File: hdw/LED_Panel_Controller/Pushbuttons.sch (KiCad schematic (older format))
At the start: 10 parts

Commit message: lots of schematic progress
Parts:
- removed U?: 74LVC1G17, TO_SOT_Packages_SMD:SOT-353_SC-70-5, symbol Custom_Library:74LVC1G17_Power
- added R?: 10k, Resistors_SMD:R_0402, symbol Custom_Library:R_Custom
- added U?: 74LVC1G97, Package_TO_SOT_SMD:SOT-363_SC-70-6, symbol Custom_Library:74LVC1G97_Power_BUF
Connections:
- net labels added: Cap_Touch_Power
- wire segments 12 -> 15
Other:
- moved on the sheet: C?, R?, SW?, U?

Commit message: made a lot more schematic progress
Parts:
- removed R?: 499, Resistors_SMD:R_0402, symbol Custom_Library:R_Custom
- added C?: 10nF, Capacitors_SMD:C_0402, symbol Custom_Library:C_Custom
- added C? (x2): 0.1uF, Capacitors_SMD:C_0402, symbol Custom_Library:C_Custom
- added C?: 10uF, Capacitors_SMD:C_0402, symbol Custom_Library:C_Custom
- added R? (x4): 1k, Resistors_SMD:R_0402, symbol Custom_Library:R_Custom
- added R? (x3): 10k, Resistors_SMD:R_0402, symbol Custom_Library:R_Custom
- added SW?: Cap_Touch, Custom Footprints Library:Capacitive_Touch_Pad, symbol Custom_Library:Cap_Touch
- added U?: AT42QT1010-TSHR, TO_SOT_Packages_SMD:SOT-23-6, symbol Sensor_Touch:AT42QT1010-TSHR
- added U?: 74LVC1G97, Package_TO_SOT_SMD:SOT-363_SC-70-6, symbol Custom_Library:74LVC1G97_Power_BUF
- C? (x4), R? (x2), U? (x2): Configuration (none) -> PUSH
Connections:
- net +3V3: now also C?.1, C?.1, U?.5 (VCC), U?.5 (VDD), U?.6 (SYNC)
- net GND: now also C?.2, C?.2, C?.2, R?.2, R?.2, U?.2 (GND), U?.2 (VSS), U?.3 (GND), U?.6 (GND)
- net at C?.2, U?.3 (SNSK): now also R?.1, R?.1
- net at SW?.1 (TP): now also R?.2, R?.2
- new net: R?.1, R?.2, U?.1 (OUT)
- new net: C?.2, R?.1, R?.1, U?.3 (SNSK)
- new net: C?.1, U?.4 (SNS)
- new net: R?.2, R?.2, SW?.1 (TP)
- new net: C?.1, R?.1, U?.1
- new net Cap_Touch_Mode: R?.1, U?.4

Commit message: added digikey pns, footprints, bom scrubbed
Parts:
- C? (x2): Digi-Key PN 490-13295-1-ND -> 399-3066-1-ND
- C? (x4): Digi-Key PN (none) -> 490-10701-1-ND
- C? (x2): Digi-Key PN 490-13211-1-ND -> 1276-1451-1-ND
- R? (x4): Digi-Key PN (none) -> RMCF0402FT1K00CT-ND
- U? (x2): Digi-Key PN (none) -> 1727-1772-1-ND
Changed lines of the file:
@@
 F 2 "Capacitors_SMD:C_0402" H 4038 1660 50  0001 C CNN
 F 3 "" H 4025 1910 50  0001 C CNN
-F 4 "490-13295-1-ND" H -790 -410 50  0001 C CNN "Digi-Key PN"
+F 4 "399-3066-1-ND" H -790 -410 50  0001 C CNN "Digi-Key PN"
 F 5 "0402" V 3610 1810 50  0000 C CNN "display_footprint"
 F 6 "50V" V 3510 1810 50  0000 C CNN "Voltage"
@@
 F 6 "X7R" H 7070 2170 50  0000 R CNN "Dielectric"
 F 7 "PUSH" H 7070 2090 50  0000 R CNN "Configuration"
+F 8 "490-10701-1-ND" H 7220 2270 50  0001 C CNN "Digi-Key PN"
 	1    7220 2270
 	1    0    0    -1
@@
 F 5 "6.3V" H 6300 2100 50  0000 R CNN "Voltage"
 F 6 "X5R" H 6300 2000 50  0000 R CNN "Dielectric"
-F 7 "490-13211-1-ND" H 6450 2100 50  0001 C CNN "Digi-Key PN"
+F 7 "1276-1451-1-ND" H 6450 2100 50  0001 C CNN "Digi-Key PN"
 F 8 "PUSH" H 6300 1920 50  0000 R CNN "Configuration"
 	1    6450 2100
@@
 F 3 "http://www.ti.com/lit/ds/symlink/sn74lvc1g97.pdf" H 7040 1810 50  0001 C CNN
 F 4 "PUSH" H 7150 1730 50  0000 C CNN "Configuration"
+F 5 "1727-1772-1-ND" H 6990 1810 50  0001 C CNN "Digi-Key PN"
 	1    6990 1810
 	1    0    0    -1
@@
 F 6 "X7R" H 4780 2440 50  0000 R CNN "Dielectric"
 F 7 "PUSH" H 4790 2720 50  0000 R CNN "Configuration"
+F 8 "490-10701-1-ND" H 4930 2540 50  0001 C CNN "Digi-Key PN"
 	1    4930 2540
 	1    0    0    -1
@@
 F 6 "1/16W" V 3500 1890 50  0000 C CNN "Wattage"
 F 7 "PUSH" V 3590 1890 50  0000 C CNN "Configuration"
+F 8 "RMCF0402FT1K00CT-ND" H 3200 1890 50  0001 C CNN "Digi-Key PN"
 	1    3200 1890
 	0    1    1    0
@@
 F 6 "1/16W" V 3500 1610 50  0000 C CNN "Wattage"
 F 7 "PUSH" V 3590 1610 50  0000 C CNN "Configuration"
+F 8 "RMCF0402FT1K00CT-ND" H 3200 1610 50  0001 C CNN "Digi-Key PN"
 	1    3200 1610
 	0    1    -1   0
@@
 F 2 "Capacitors_SMD:C_0402" H 4038 3660 50  0001 C CNN
 F 3 "" H 4025 3910 50  0001 C CNN
-F 4 "490-13295-1-ND" H -790 1590 50  0001 C CNN "Digi-Key PN"
+F 4 "399-3066-1-ND" H -790 1590 50  0001 C CNN "Digi-Key PN"
 F 5 "0402" V 3610 3810 50  0000 C CNN "display_footprint"
 F 6 "50V" V 3510 3810 50  0000 C CNN "Voltage"
@@
 F 6 "X7R" H 7070 4170 50  0000 R CNN "Dielectric"
 F 7 "PUSH" H 7070 4090 50  0000 R CNN "Configuration"
+F 8 "490-10701-1-ND" H 7220 4270 50  0001 C CNN "Digi-Key PN"
 	1    7220 4270
 	1    0    0    -1
@@
 F 5 "6.3V" H 6300 4100 50  0000 R CNN "Voltage"
 F 6 "X5R" H 6300 4000 50  0000 R CNN "Dielectric"
-F 7 "490-13211-1-ND" H 6450 4100 50  0001 C CNN "Digi-Key PN"
+F 7 "1276-1451-1-ND" H 6450 4100 50  0001 C CNN "Digi-Key PN"
 F 8 "PUSH" H 6300 3920 50  0000 R CNN "Configuration"
 	1    6450 4100
@@
 F 3 "http://www.ti.com/lit/ds/symlink/sn74lvc1g97.pdf" H 7040 3810 50  0001 C CNN
 F 4 "PUSH" H 7150 3730 50  0000 C CNN "Configuration"
+F 5 "1727-1772-1-ND" H 6990 3810 50  0001 C CNN "Digi-Key PN"
 	1    6990 3810
 	1    0    0    -1
@@
 F 6 "X7R" H 4780 4440 50  0000 R CNN "Dielectric"
 F 7 "PUSH" H 4790 4720 50  0000 R CNN "Configuration"
+F 8 "490-10701-1-ND" H 4930 4540 50  0001 C CNN "Digi-Key PN"
 	1    4930 4540
 	1    0    0    -1
@@
 F 6 "1/16W" V 3500 3890 50  0000 C CNN "Wattage"
 F 7 "PUSH" V 3590 3890 50  0000 C CNN "Configuration"
+F 8 "RMCF0402FT1K00CT-ND" H 3200 3890 50  0001 C CNN "Digi-Key PN"
 	1    3200 3890
 	0    1    1    0
@@
 F 6 "1/16W" V 3500 3610 50  0000 C CNN "Wattage"
 F 7 "PUSH" V 3590 3610 50  0000 C CNN "Configuration"
+F 8 "RMCF0402FT1K00CT-ND" H 3200 3610 50  0001 C CNN "Digi-Key PN"
 	1    3200 3610
 	0    1    -1   0

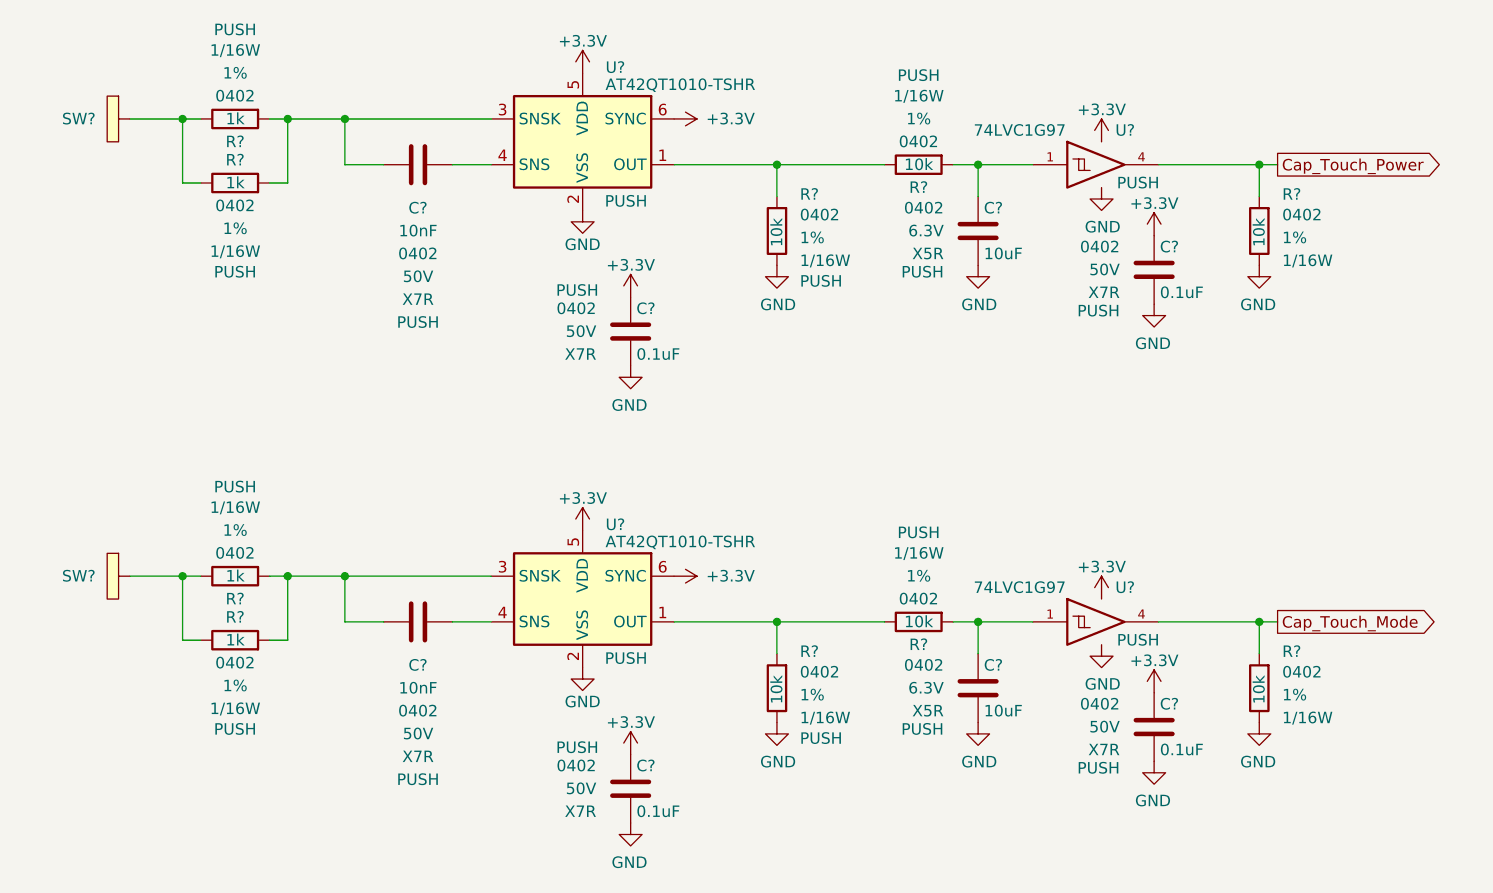
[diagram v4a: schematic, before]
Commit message: assigned I2C addresses
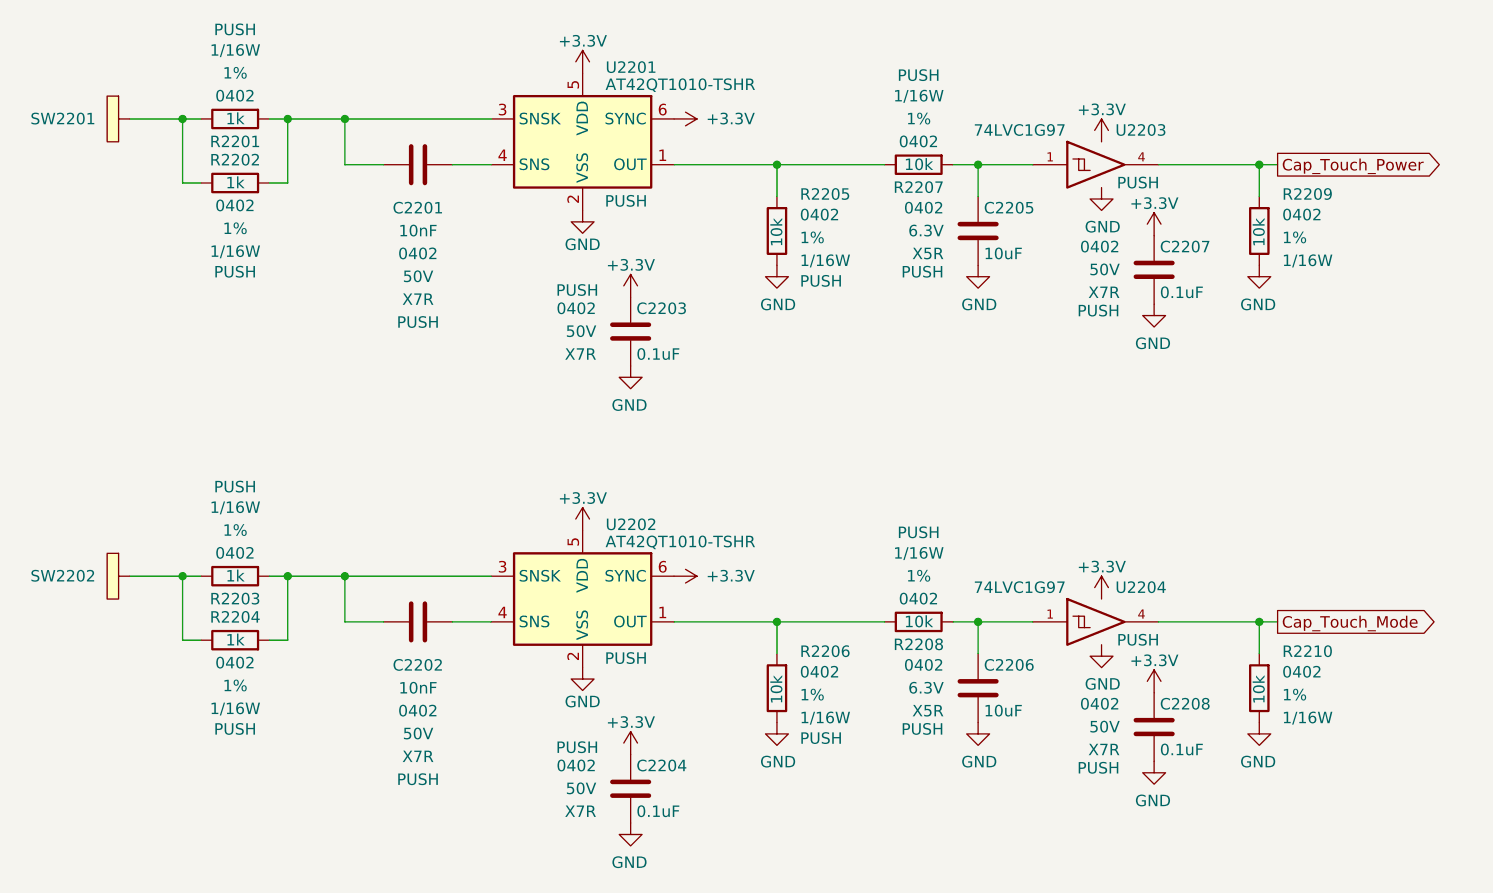
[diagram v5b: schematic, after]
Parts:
- gave numbers to parts that had none: 24

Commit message: added BOMs, some consolidation
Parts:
- C2203, C2204, C2207, C2208: Digi-Key PN 490-10701-1-ND -> 490-10698-1-ND
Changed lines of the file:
@@
 F 6 "X7R" H 7070 2170 50  0000 R CNN "Dielectric"
 F 7 "PUSH" H 7070 2090 50  0000 R CNN "Configuration"
-F 8 "490-10701-1-ND" H 7220 2270 50  0001 C CNN "Digi-Key PN"
+F 8 "490-10698-1-ND" H 7220 2270 50  0001 C CNN "Digi-Key PN"
 	1    7220 2270
 	1    0    0    -1
@@
 F 6 "X7R" H 4780 2440 50  0000 R CNN "Dielectric"
 F 7 "PUSH" H 4790 2720 50  0000 R CNN "Configuration"
-F 8 "490-10701-1-ND" H 4930 2540 50  0001 C CNN "Digi-Key PN"
+F 8 "490-10698-1-ND" H 4930 2540 50  0001 C CNN "Digi-Key PN"
 	1    4930 2540
 	1    0    0    -1
@@
 F 6 "X7R" H 7070 4170 50  0000 R CNN "Dielectric"
 F 7 "PUSH" H 7070 4090 50  0000 R CNN "Configuration"
-F 8 "490-10701-1-ND" H 7220 4270 50  0001 C CNN "Digi-Key PN"
+F 8 "490-10698-1-ND" H 7220 4270 50  0001 C CNN "Digi-Key PN"
 	1    7220 4270
 	1    0    0    -1
@@
 F 6 "X7R" H 4780 4440 50  0000 R CNN "Dielectric"
 F 7 "PUSH" H 4790 4720 50  0000 R CNN "Configuration"
-F 8 "490-10701-1-ND" H 4930 4540 50  0001 C CNN "Digi-Key PN"
+F 8 "490-10698-1-ND" H 4930 4540 50  0001 C CNN "Digi-Key PN"
 	1    4930 4540
 	1    0    0    -1
